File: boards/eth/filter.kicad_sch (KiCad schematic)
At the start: 12 parts, among them U21 74HC86, U22 74HC21, U23 74HC21, U24 74HC74, U3 74HC32, U6 74HC74, U7 74HC08

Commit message: Eth: schematics checked
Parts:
- C34: renamed from C5; footprint (none) -> Capacitor_SMD:C_0805_2012Metric
- C35: renamed from C6; footprint (none) -> Capacitor_SMD:C_0805_2012Metric
- C36: renamed from C7; footprint (none) -> Capacitor_SMD:C_0805_2012Metric
- C37: renamed from C8; footprint (none) -> Capacitor_SMD:C_0805_2012Metric
- C38: renamed from C9; footprint (none) -> Capacitor_SMD:C_0805_2012Metric
- U10: renamed from U6; footprint (none) -> Package_SO:TSSOP-14_4.4x5mm_P0.65mm
- U33: renamed from U21; footprint (none) -> Package_SO:TSSOP-14_4.4x5mm_P0.65mm
- U34: renamed from U22; footprint (none) -> Package_SO:TSSOP-14_4.4x5mm_P0.65mm
- U35: renamed from U23; footprint (none) -> Package_SO:TSSOP-14_4.4x5mm_P0.65mm
- U36: renamed from U24; footprint (none) -> Package_SO:TSSOP-14_4.4x5mm_P0.65mm
- U5: renamed from U3; footprint (none) -> Package_SO:TSSOP-14_4.4x5mm_P0.65mm
- U6: renamed from U7; footprint (none) -> Package_SO:TSSOP-14_4.4x5mm_P0.65mm

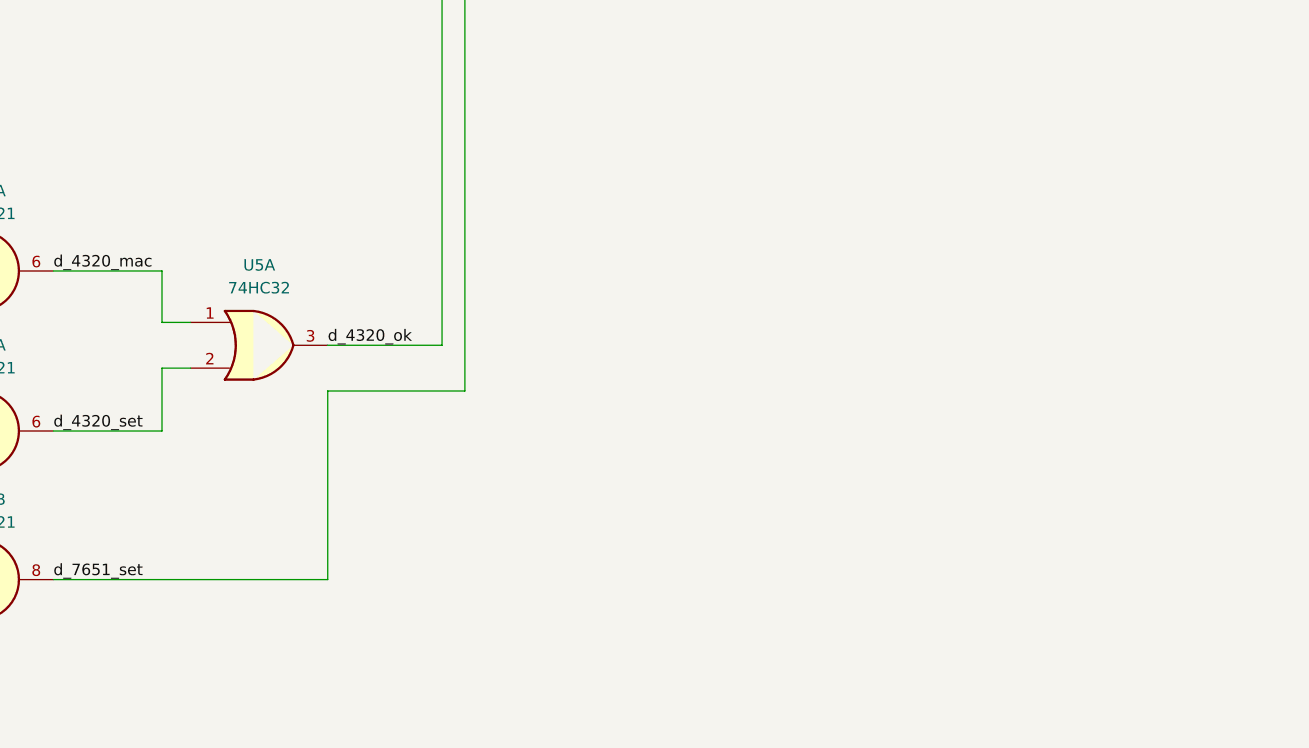
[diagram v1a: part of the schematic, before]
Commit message: Eth: untangle schematic
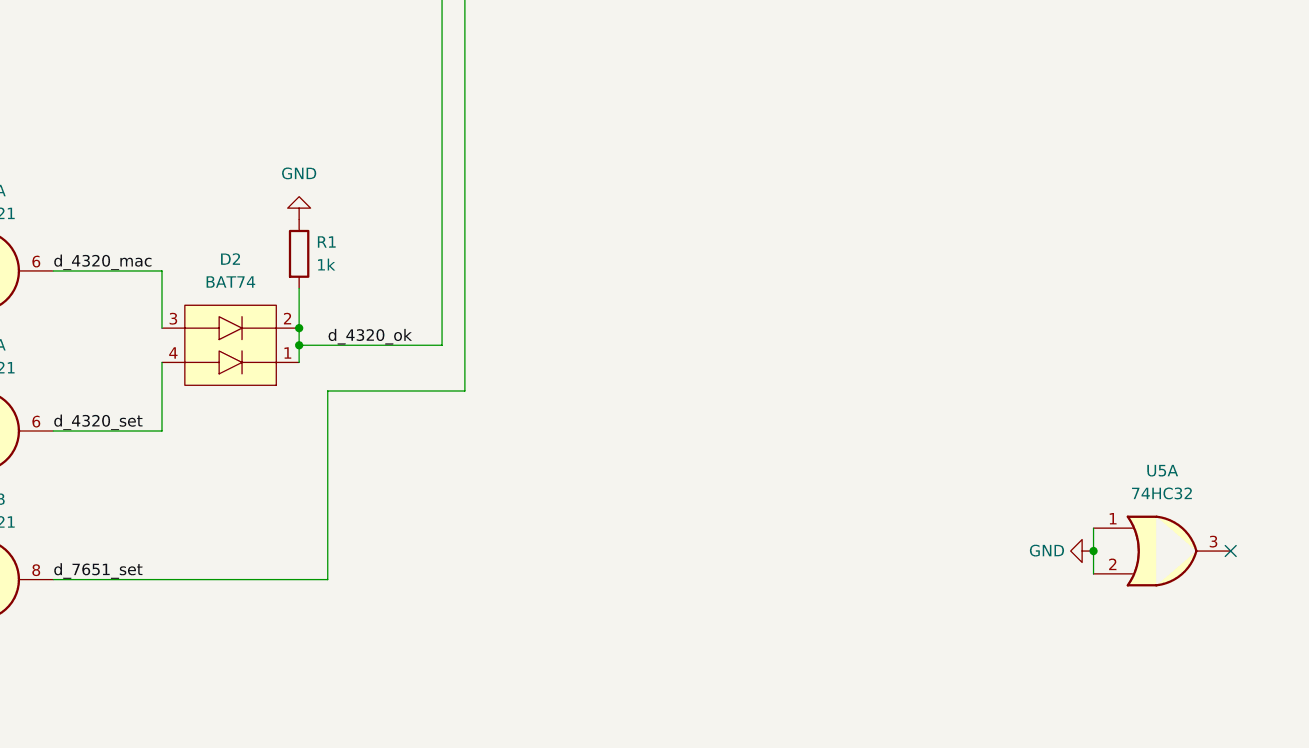
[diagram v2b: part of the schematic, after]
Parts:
- added D2: BAT74, Package_TO_SOT_SMD:SOT-143, symbol eth:BAT74
- added R1: 1k, Resistor_SMD:R_0805_2012Metric, symbol Device:R
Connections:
- net GND: now also U5.1, U5.2, R1.1
- net d_4320_mac: now also D2.3 (A2); no longer U5.1
- net d_4320_ok: now also D2.1 (C1), D2.2 (C2), R1.2; no longer U5.3
- net d_4320_set: now also D2.4 (A1); no longer U5.2
- no-connect marks 3 -> 4
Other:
- moved on the sheet: U5A
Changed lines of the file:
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@@
     (rev "1")
   )
+  (junction (at 325.755 189.23) (diameter 0) (color 0 0 0 0)
+  )
   (junction (at 187.325 76.835) (diameter 0) (color 0 0 0 0)
   )
@@
   )
   (junction (at 258.445 76.835) (diameter 0) (color 0 0 0 0)
+  )
+  (junction (at 237.49 164.465) (diameter 0) (color 0 0 0 0)
+  )
+  (junction (at 237.49 166.37) (diameter 0) (color 0 0 0 0)
   )
   (no_connect (at 315.595 107.95))
   (no_connect (at 285.115 110.49))
   (no_connect (at 194.945 86.995))
+  (no_connect (at 340.995 189.23))
   (bus_entry (at 182.245 172.085) (size 2.54 2.54)
     (stroke (width 0) (type default))
@@
     (stroke (width 0) (type default))
   )
+  (wire (pts (xy 237.49 166.37) (xy 253.365 166.37))
+    (stroke (width 0) (type default))
+  )
   (wire (pts (xy 295.91 102.87) (xy 300.355 102.87))
     (stroke (width 0) (type default))
@@
     (stroke (width 0) (type default))
   )
+  (wire (pts (xy 325.755 189.23) (xy 325.755 191.77))
+    (stroke (width 0) (type default))
+  )
   (wire (pts (xy 180.975 148.59) (xy 172.72 148.59))
     (stroke (width 0) (type default))
@@
     (stroke (width 0) (type default))
   )
+  (wire (pts (xy 325.755 186.69) (xy 325.755 189.23))
+    (stroke (width 0) (type default))
+  )
   (wire (pts (xy 184.785 177.165) (xy 194.945 177.165))
     (stroke (width 0) (type default))
@@
     (stroke (width 0) (type default))
   )
+  (wire (pts (xy 237.49 166.37) (xy 237.49 168.275))
+    (stroke (width 0) (type default))
+  )
   (bus (pts (xy 142.24 156.845) (xy 142.24 169.545))
     (stroke (width 0) (type default))
   )
+  (wire (pts (xy 237.49 164.465) (xy 237.49 166.37))
+    (stroke (width 0) (type default))
+  )
   (bus (pts (xy 149.86 128.27) (xy 149.86 143.51))
     (stroke (width 0) (type default))
@@
     (stroke (width 0) (type default))
   )
-  (wire (pts (xy 222.25 163.83) (xy 225.425 163.83))
-    (stroke (width 0) (type default))
-  )
   (wire (pts (xy 186.055 154.305) (xy 194.945 154.305))
     (stroke (width 0) (type default))
@@
     (stroke (width 0) (type default))
   )
-  (wire (pts (xy 240.665 166.37) (xy 253.365 166.37))
-    (stroke (width 0) (type default))
-  )
   (wire (pts (xy 121.92 84.455) (xy 179.705 84.455))
     (stroke (width 0) (type default))
@@
     (stroke (width 0) (type default))
   )
-  (wire (pts (xy 222.25 168.91) (xy 225.425 168.91))
-    (stroke (width 0) (type default))
-  )
   (bus (pts (xy 208.915 102.87) (xy 208.915 107.95))
     (stroke (width 0) (type default))
@@
     (stroke (width 0) (type default))
   )
-  (wire (pts (xy 222.25 158.115) (xy 222.25 163.83))
-    (stroke (width 0) (type default))
-  )
   (bus (pts (xy 182.245 174.625) (xy 182.245 177.165))
     (stroke (width 0) (type default))
@@
     (stroke (width 0) (type default))
   )
+  (wire (pts (xy 222.25 158.115) (xy 222.25 164.465))
+    (stroke (width 0) (type default))
+  )
   (bus (pts (xy 142.24 169.545) (xy 182.245 169.545))
     (stroke (width 0) (type default))
@@
     (stroke (width 0) (type default))
   )
+  (wire (pts (xy 237.49 160.02) (xy 237.49 164.465))
+    (stroke (width 0) (type default))
+  )
   (wire (pts (xy 152.4 146.05) (xy 157.48 146.05))
     (stroke (width 0) (type default))
@@
     (stroke (width 0) (type default))
   )
+  (wire (pts (xy 222.25 168.275) (xy 222.25 175.895))
+    (stroke (width 0) (type default))
+  )
   (wire (pts (xy 122.555 76.835) (xy 187.325 76.835))
     (stroke (width 0) (type default))
@@
   )
   (bus (pts (xy 182.245 177.165) (xy 182.245 186.055))
-    (stroke (width 0) (type default))
-  )
-  (wire (pts (xy 222.25 175.895) (xy 222.25 168.91))
     (stroke (width 0) (type default))
   )
@@
     )
   )
-  (symbol (lib_id "74xx:74LS32") (at 233.045 166.37 0) (unit 1)
-    (in_bom yes) (on_board yes) (dnp no) (fields_autoplaced)
-    (property "Reference" "U5" (at 233.045 157.48 0)
-      (effects (font (size 1.27 1.27)))
-    )
-    (property "Value" "74HC32" (at 233.045 160.02 0)
-      (effects (font (size 1.27 1.27)))
-    )
-    (property "Footprint" "Package_SO:TSSOP-14_4.4x5mm_P0.65mm" (at 233.045 166.37 0)
-      (effects (font (size 1.27 1.27)) hide)
-    )
-    (property "Datasheet" "http://www.ti.com/lit/gpn/sn74LS32" (at 233.045 166.37 0)
+  (symbol (lib_id "74xx:74LS32") (at 333.375 189.23 0) (unit 1)
+    (in_bom yes) (on_board yes) (dnp no) (fields_autoplaced)
+    (property "Reference" "U5" (at 333.375 180.34 0)
+      (effects (font (size 1.27 1.27)))
+    )
+    (property "Value" "74HC32" (at 333.375 182.88 0)
+      (effects (font (size 1.27 1.27)))
+    )
+    (property "Footprint" "Package_SO:TSSOP-14_4.4x5mm_P0.65mm" (at 333.375 189.23 0)
+      (effects (font (size 1.27 1.27)) hide)
+    )
+    (property "Datasheet" "http://www.ti.com/lit/gpn/sn74LS32" (at 333.375 189.23 0)
       (effects (font (size 1.27 1.27)) hide)
     )
@@
     )
   )
+  (symbol (lib_id "Device:R") (at 237.49 156.21 0) (unit 1)
+    (in_bom yes) (on_board yes) (dnp no) (fields_autoplaced)
+    (property "Reference" "R1" (at 239.395 154.94 0)
+      (effects (font (size 1.27 1.27)) (justify left))
+    )
+    (property "Value" "1k" (at 239.395 157.48 0)
+      (effects (font (size 1.27 1.27)) (justify left))
+    )
+    (property "Footprint" "Resistor_SMD:R_0805_2012Metric" (at 235.712 156.21 90)
+      (effects (font (size 1.27 1.27)) hide)
+    )
+    (property "Datasheet" "~" (at 237.49 156.21 0)
+      (effects (font (size 1.27 1.27)) hide)
+    )
+    (pin "1")
+    (pin "2")
+    (instances
+      (project "eth"
+        (path "/25b810b6-8afb-4eb4-8eaf-dfe3b666cbdb"
+          (reference "R1") (unit 1)
+        )
+        (path "/25b810b6-8afb-4eb4-8eaf-dfe3b666cbdb/39e18fc2-9d3f-4915-a4a0-511df53a2759"
+          (reference "R6") (unit 1)
+        )
+      )
+    )
+  )
   (symbol (lib_id "power:VCC") (at 266.065 220.345 0) (unit 1)
     (in_bom yes) (on_board yes) (dnp no) (fields_autoplaced)
@@
     )
   )
+  (symbol (lib_id "power:GND") (at 325.755 189.23 270) (unit 1)
+    (in_bom yes) (on_board yes) (dnp no) (fields_autoplaced)
+    (property "Reference" "#PWR0218" (at 319.405 189.23 0)
+      (effects (font (size 1.27 1.27)) hide)
+    )
+    (property "Value" "GND" (at 322.58 189.23 90)
+      (effects (font (size 1.27 1.27)) (justify right))
+    )
+    (property "Footprint" "" (at 325.755 189.23 0)
+      (effects (font (size 1.27 1.27)) hide)
+    )
+    (property "Datasheet" "" (at 325.755 189.23 0)
+      (effects (font (size 1.27 1.27)) hide)
+    )
+    (pin "1")
+    (instances
+      (project "eth"
+        (path "/25b810b6-8afb-4eb4-8eaf-dfe3b666cbdb/39e18fc2-9d3f-4915-a4a0-511df53a2759"
+          (reference "#PWR0218") (unit 1)
+        )
+      )
+    )
+  )
   (symbol (lib_id "power:VCC") (at 234.95 243.84 0) (unit 1)
     (in_bom yes) (on_board yes) (dnp no) (fields_autoplaced)
@@
         (path "/25b810b6-8afb-4eb4-8eaf-dfe3b666cbdb/39e18fc2-9d3f-4915-a4a0-511df53a2759"
           (reference "#PWR0188") (unit 1)
+        )
+      )
+    )
+  )
+  (symbol (lib_id "power:GND") (at 237.49 152.4 180) (unit 1)
+    (in_bom yes) (on_board yes) (dnp no) (fields_autoplaced)
+    (property "Reference" "#PWR0216" (at 237.49 146.05 0)
+      (effects (font (size 1.27 1.27)) hide)
+    )
+    (property "Value" "GND" (at 237.49 147.32 0)
+      (effects (font (size 1.27 1.27)))
+    )
+    (property "Footprint" "" (at 237.49 152.4 0)
+      (effects (font (size 1.27 1.27)) hide)
+    )
+    (property "Datasheet" "" (at 237.49 152.4 0)
+      (effects (font (size 1.27 1.27)) hide)
+    )
+    (pin "1")
+    (instances
+      (project "eth"
+        (path "/25b810b6-8afb-4eb4-8eaf-dfe3b666cbdb/39e18fc2-9d3f-4915-a4a0-511df53a2759"
+          (reference "#PWR0216") (unit 1)
         )
       )
@@
         )
       )
+    )
+  )
+  (symbol (lib_id "eth:BAT74") (at 229.87 167.005 180) (unit 1)
+    (in_bom yes) (on_board yes) (dnp no) (fields_autoplaced)
+    (property "Reference" "D2" (at 229.87 156.845 0)
+      (effects (font (size 1.27 1.27)))
+    )
+    (property "Value" "BAT74" (at 229.87 159.385 0)
+      (effects (font (size 1.27 1.27)))
+    )
+    (property "Footprint" "Package_TO_SOT_SMD:SOT-143" (at 232.41 155.575 0)
+      (effects (font (size 1.27 1.27)) hide)
+    )
+    (property "Datasheet" "https://www.mouser.de/datasheet/2/916/BAT74-2937432.pdf" (at 231.14 158.115 0)
+      (effects (font (size 1.27 1.27)) hide)
+    )
+    (pin "1")
+    (pin "2")
+    (pin "3")
+    (pin "4")
+    (instances
+      (project "eth"
+        (path "/25b810b6-8afb-4eb4-8eaf-dfe3b666cbdb"
+          (reference "D2") (unit 1)
+        )
+        (path "/25b810b6-8afb-4eb4-8eaf-dfe3b666cbdb/39e18fc2-9d3f-4915-a4a0-511df53a2759"
+          (reference "D7") (unit 1)
+        )
+      )
